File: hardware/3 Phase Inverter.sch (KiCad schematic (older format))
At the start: 21 parts, among them Q2 NTD5806N, Q3 NTD5806N, Q4 NTD5806N, Q5 NTD5806N, Q6 NTD5806N, Q7 NTD5806N, U5 IRS2301S, U6 IRS2301S, U7 IRS2301S

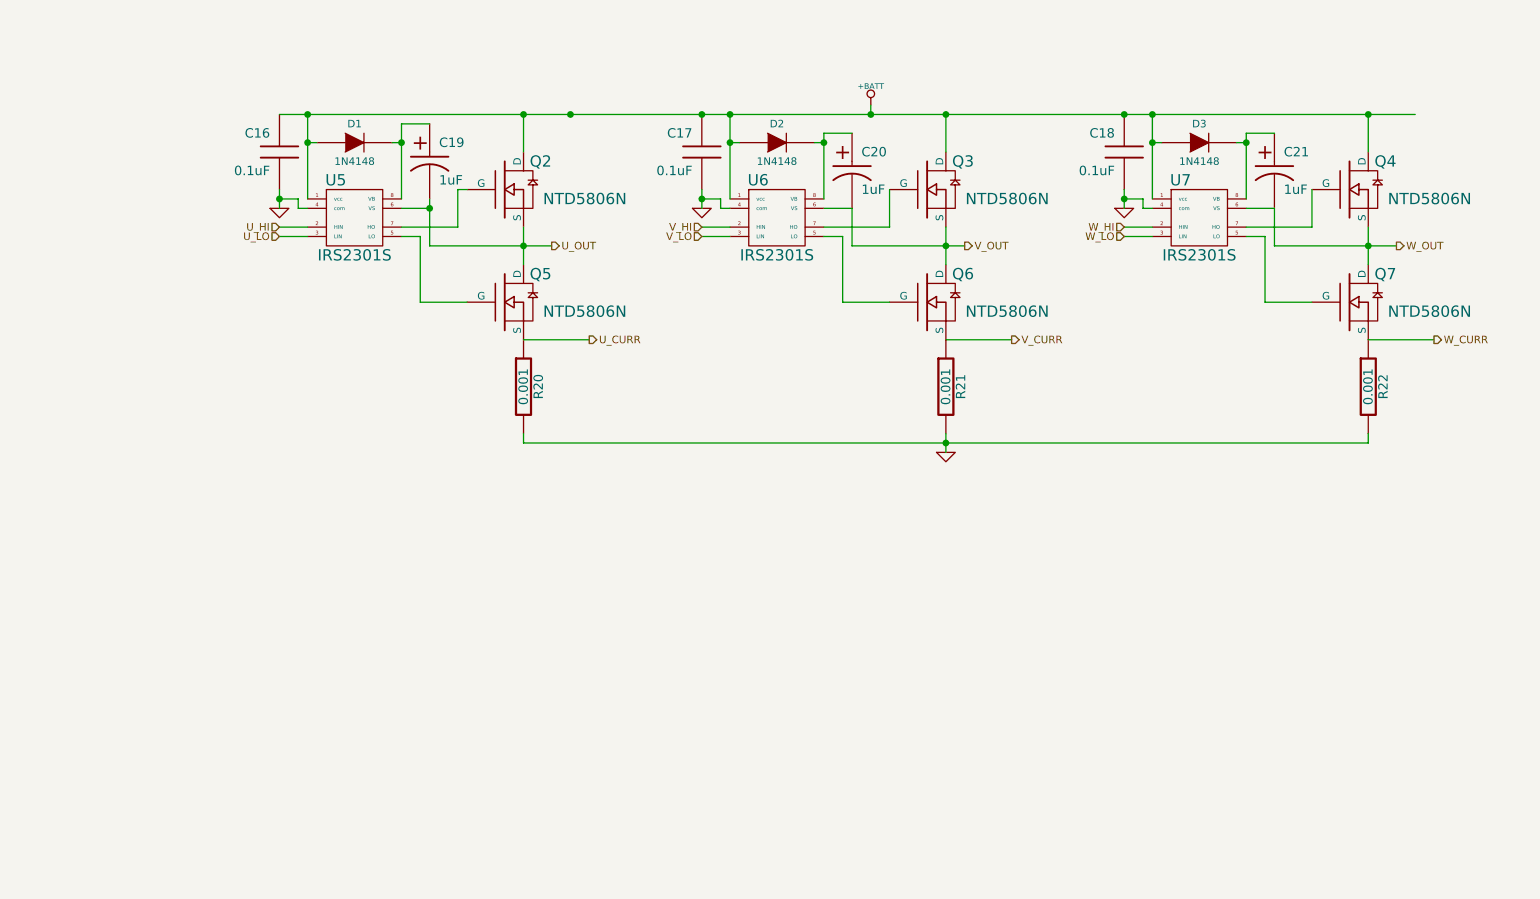
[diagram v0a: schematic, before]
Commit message: Modified the components in the 3 phase inverter
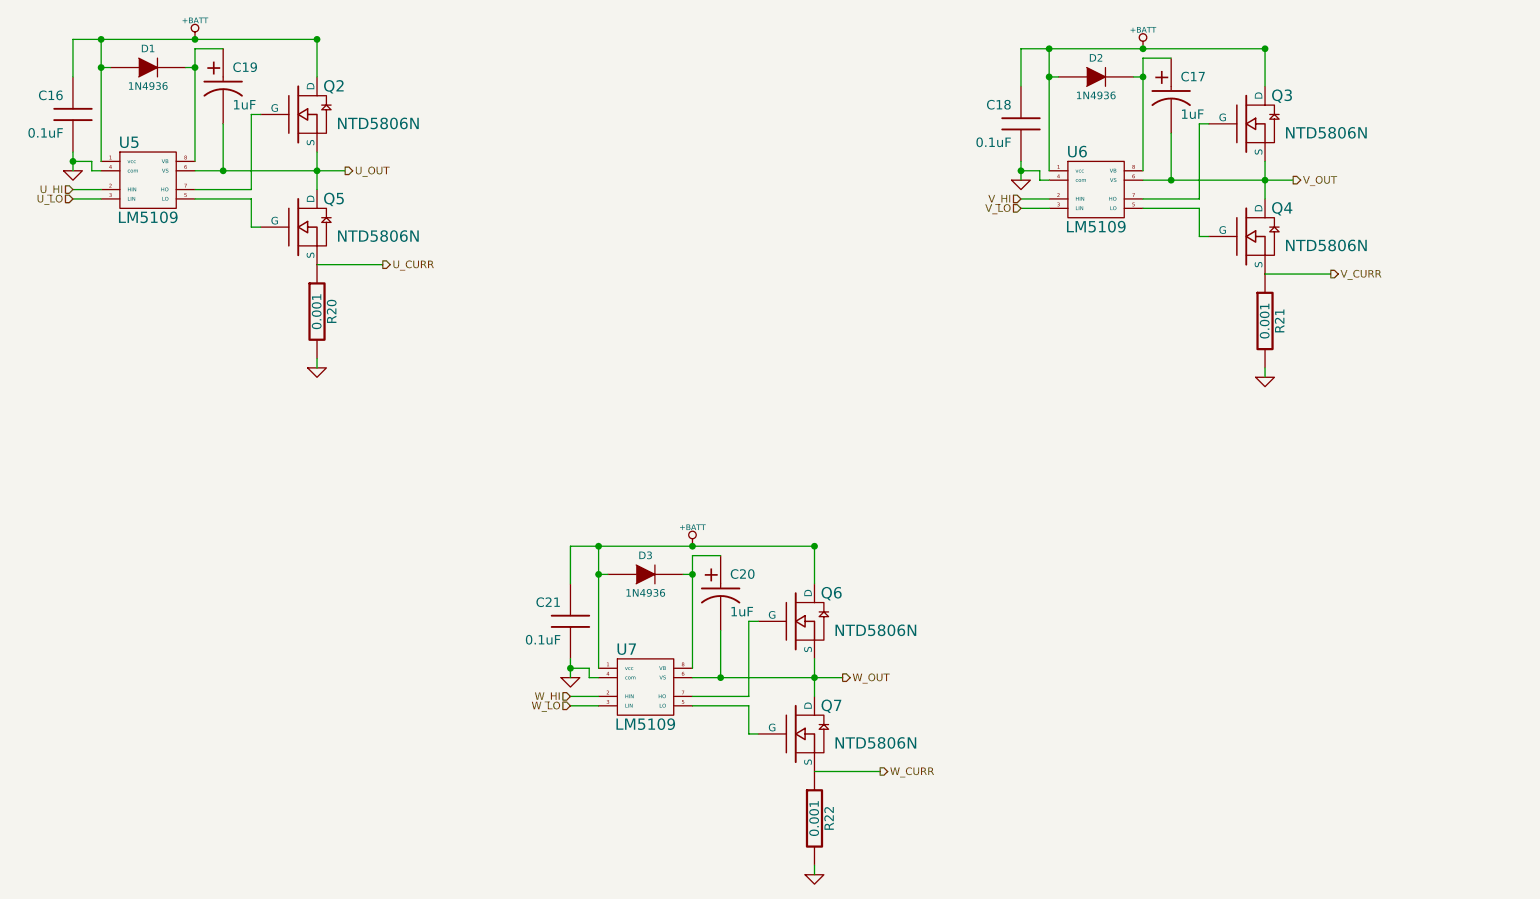
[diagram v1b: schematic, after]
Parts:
- removed C17: 0.1uF, 0805, symbol C
- removed C21: 1uF, symbol CP1
- added C17: 1uF, symbol CP1
- added C21: 0.1uF, 0805, symbol C
- D1, D2, D3: value 1N4148 -> 1N4936
- U5, U6, U7: value IRS2301S -> LM5109; Digikey P/N IRS2301SPBF-ND -> LM5109MA/NOPB-ND; Mfg P/N IRS2301SPBF -> LM5109MA/NOPB; Mouser P/N 942-IRS2301SPBF -> 926-LM5109MA/NOPB
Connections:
- net +BATT: now also Q6.D, C21.1; no longer Q4.D
- net GND: now also C21.2
- net V_CURR: now also Q4.S; no longer Q6.S
- net V_OUT: now also Q4.D, C17.2; no longer C20.2, Q6.D
- net W_OUT: now also C20.2, Q6.S; no longer Q4.S
- net at Q4.G: now also U6.5 (LO); no longer U7.7 (HO)
- net at D3.2 (K), U7.8 (VB): now also C20.1
- net at Q6.G: now also U7.7 (HO); no longer U6.5 (LO)
- net at D2.2 (K), U6.8 (VB): now also C17.1; no longer C20.1
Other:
- moved on the sheet: C16, C19, D1, Q2, Q5, R20, U5

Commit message: Updated the Part number and footprints for most components
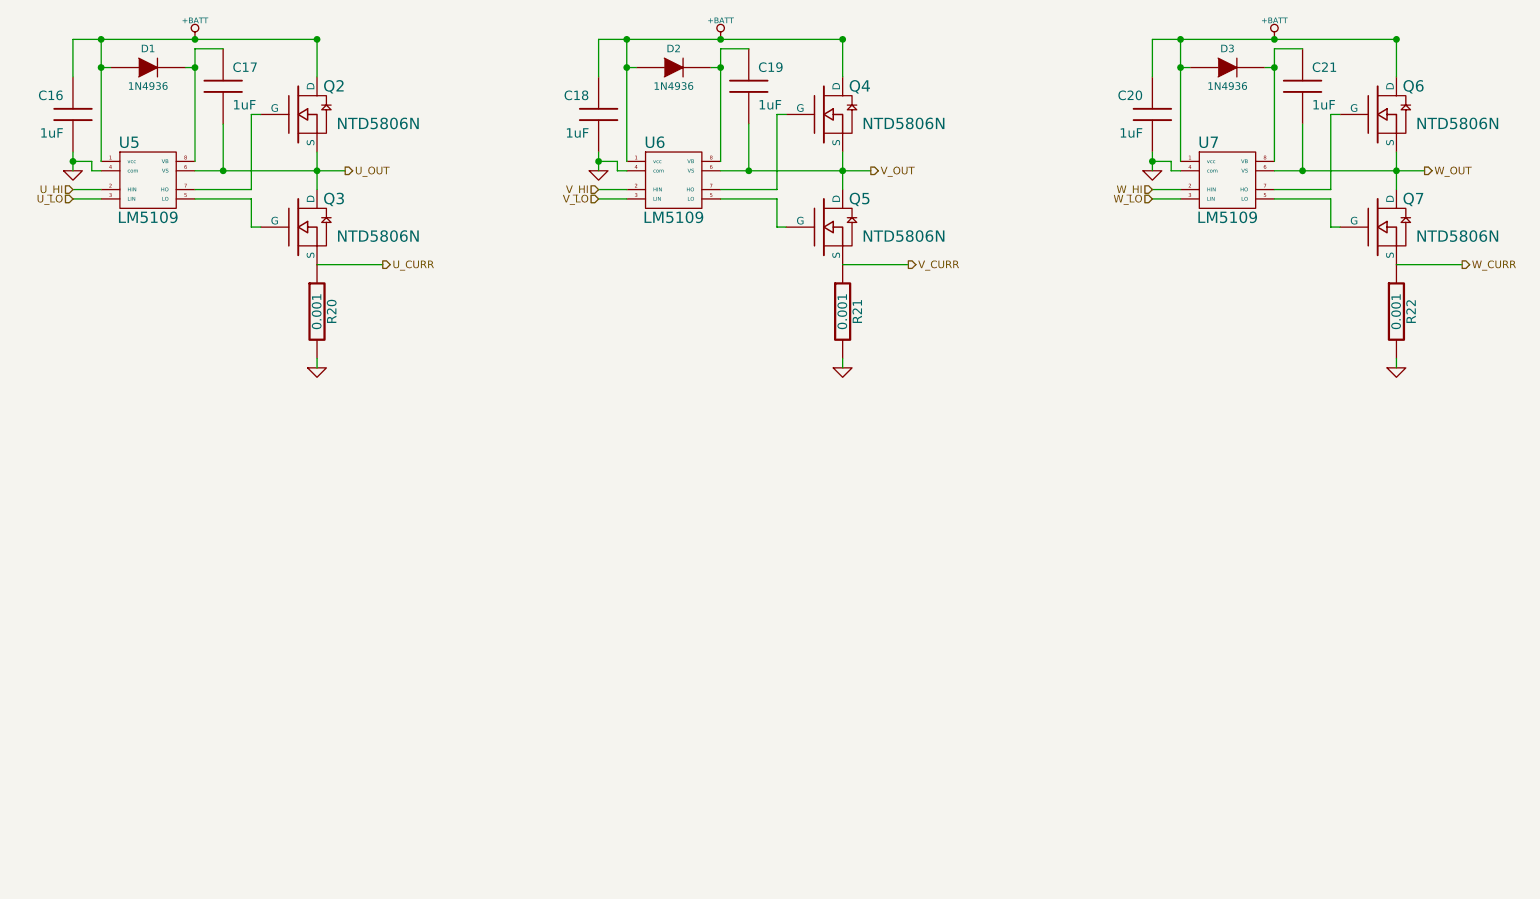
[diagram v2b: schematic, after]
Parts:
- removed C17, C19, C20: 1uF, symbol CP1
- added C17, C19, C20: 1uF, 0805, symbol C
- C16, C18, C21: value 0.1uF -> 1uF; Digikey P/N (none) -> 1276-3010-1-ND; Mfg P/N (none) -> CL21F105ZBFNNNE
- D1, D2, D3: footprint DO-35 -> DO-41; Digikey P/N (none) -> 1N4936FSCT-ND; Mfg P/N (none) -> 1N4936; Mouser P/N (none) -> 512-1N4936
- Q2, Q3, Q4, Q5, Q6, Q7: Digikey P/N (none) -> NTD5806NT4GOSCT-ND; Mfg P/N (none) -> NTD5806NT4G; Mouser P/N (none) -> 863-NTD5806NT4G
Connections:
- net +BATT: now also Q4.D, C20.1; no longer C21.1, Q3.D
- net GND: now also C20.2; no longer C21.2
- net U_CURR: now also Q3.S; no longer Q5.S
- net U_OUT: now also Q3.D, C17.2; no longer Q5.D
- net V_CURR: now also Q5.S; no longer Q4.S
- net V_OUT: now also Q4.S, Q5.D, C19.2; no longer Q3.S, Q4.D
- net W_OUT: now also C21.2
- net at D1.2 (K), U5.8 (VB): now also C17.1
- net at U5.5 (LO): now also Q3.G; no longer Q5.G
- net at U6.7 (HO): now also Q4.G; no longer Q3.G
- net at U6.5 (LO): now also Q5.G; no longer Q4.G
- net at D2.2 (K), U6.8 (VB): now also C19.1
- net at D3.2 (K), U7.8 (VB): now also C21.1
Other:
- moved on the sheet: R21, R22, U6, U7
